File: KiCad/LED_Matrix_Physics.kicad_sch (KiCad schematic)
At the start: 3 parts

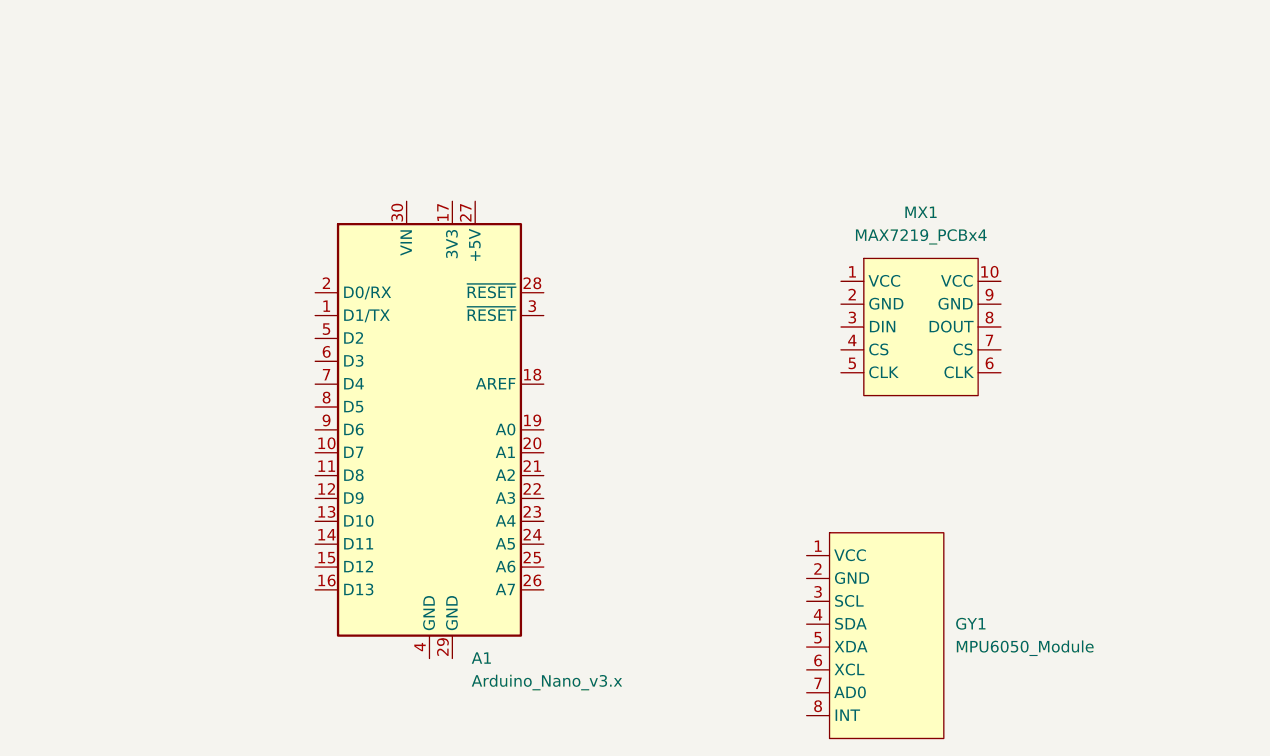
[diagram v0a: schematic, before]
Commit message: Created KiCad schematic
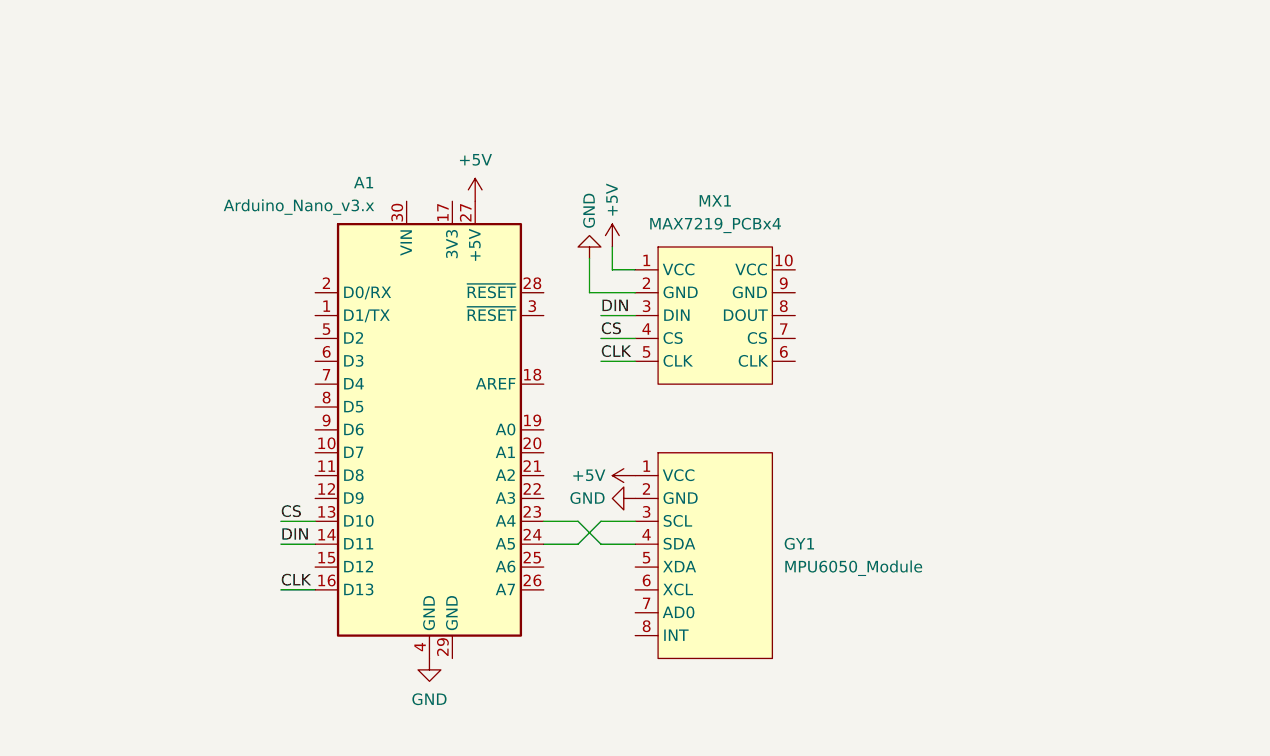
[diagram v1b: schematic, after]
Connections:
- net CS: now reaches A1.13 (D10)
- net CS: now also MX1.4 (CS)
- net DIN: now reaches A1.14 (D11)
- net DIN: now also MX1.3 (DIN)
- net CLK: now reaches A1.16 (D13)
- net CLK: now also MX1.5 (CLK)
- net at A1.23 (A4): now also GY1.4 (SDA)
- net at A1.24 (A5): now also GY1.3 (SCL)
- net +5V: now reaches A1.27 (+5V)
- net +5V: now also GY1.1 (VCC), MX1.1 (VCC)
- net GND: now reaches A1.4 (GND)
- net GND: now also GY1.2 (GND), MX1.2 (GND)
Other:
- moved on the sheet: GY1, MX1

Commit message: Added battery to schematic
Added a battery, diode for inverse polarity protection, and a switch for the battery to the schematic.
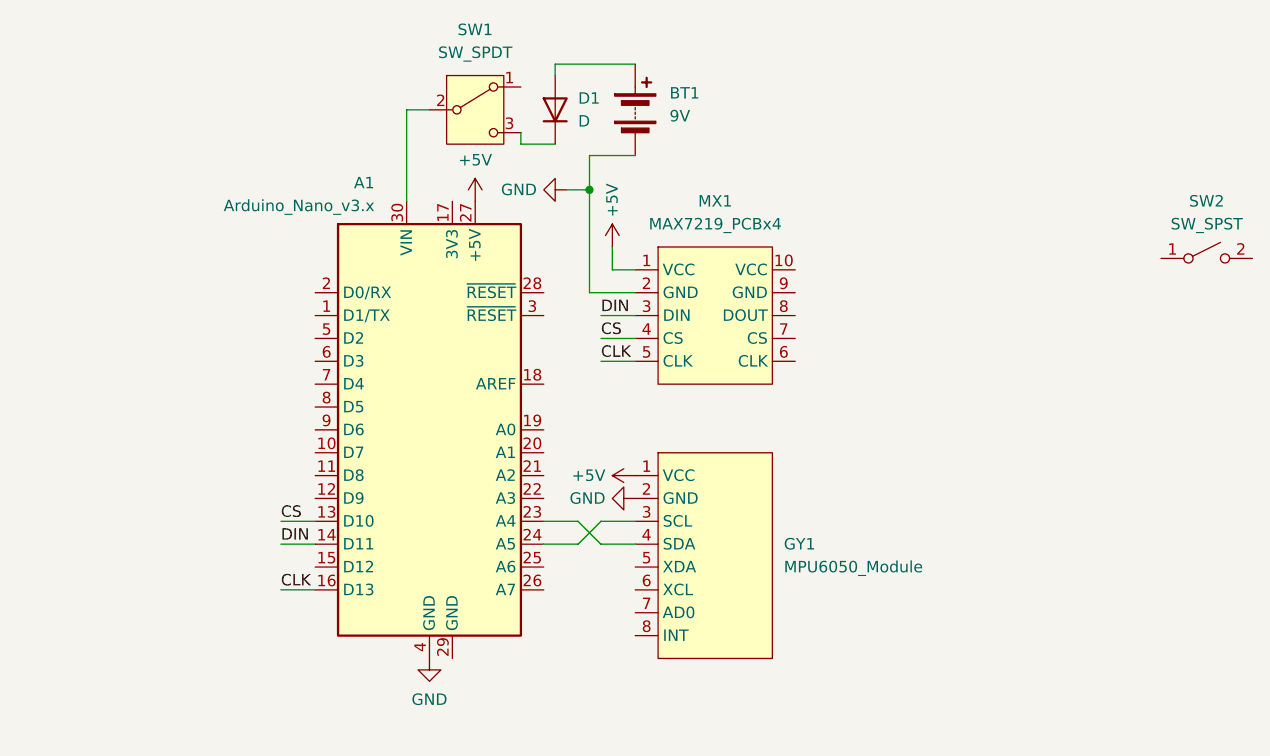
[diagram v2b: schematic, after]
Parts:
- added BT1: 9V, symbol Device:Battery
- added D1: D, symbol Device:D
- added SW1: SW_SPDT, symbol Switch:SW_SPDT
- added SW2: SW_SPST, symbol Switch:SW_SPST
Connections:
- net GND: now also BT1.2 (-)
- net at A1.30 (VIN): now also SW1.2 (B)
- new net: D1.1 (K), SW1.3 (C)
- new net: BT1.1 (+), D1.2 (A)

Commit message: Moved battery diode in schematic
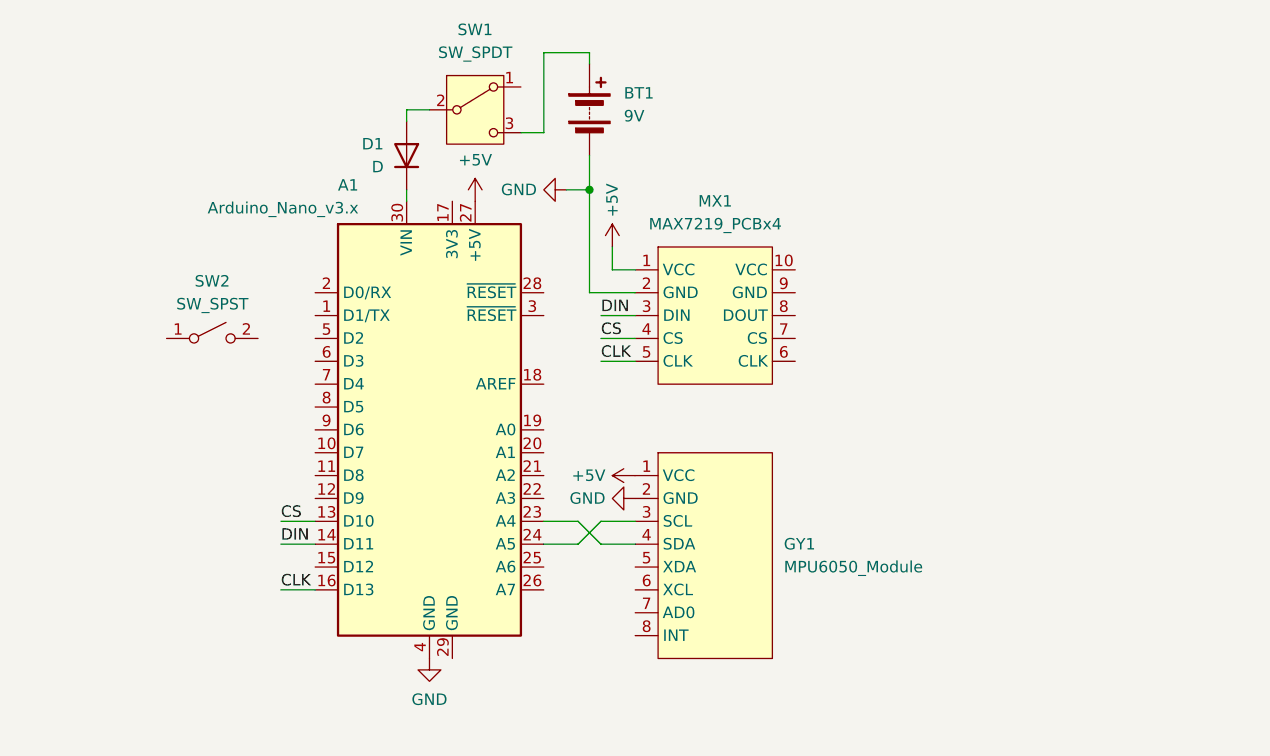
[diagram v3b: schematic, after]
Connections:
- net at A1.30 (VIN): now also D1.1 (K); no longer SW1.2 (B)
- net at SW1.3 (C): now also BT1.1 (+); no longer D1.1 (K)
- net at D1.2 (A): now also SW1.2 (B); no longer BT1.1 (+)
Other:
- moved on the sheet: BT1, D1, SW2
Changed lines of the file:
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@@
-	(wire
-		(pts
-			(xy 57.15 49.53) (xy 54.61 49.53)
-		)
-		(stroke
-			(width 0)
-			(type default)
-		)
-	)
 	(wire
 		(pts
@@
 	(wire
 		(pts
+			(xy 54.61 49.53) (xy 57.15 49.53)
+		)
+		(stroke
+			(width 0)
+			(type default)
+		)
+	)
+	(wire
+		(pts
 			(xy 76.2 72.39) (xy 80.01 72.39)
 		)
@@
 	(wire
 		(pts
-			(xy 80.01 44.45) (xy 71.12 44.45)
+			(xy 74.93 43.18) (xy 69.85 43.18)
 		)
 		(stroke
@@
 	(wire
 		(pts
-			(xy 67.31 53.34) (xy 67.31 52.07)
+			(xy 54.61 58.42) (xy 54.61 59.69)
+		)
+		(stroke
+			(width 0)
+			(type default)
+		)
+	)
+	(wire
+		(pts
+			(xy 74.93 43.18) (xy 74.93 44.45)
 		)
 		(stroke
@@
 	(wire
 		(pts
-			(xy 71.12 44.45) (xy 71.12 45.72)
+			(xy 69.85 43.18) (xy 69.85 52.07)
+		)
+		(stroke
+			(width 0)
+			(type default)
+		)
+	)
+	(wire
+		(pts
+			(xy 54.61 50.8) (xy 54.61 49.53)
 		)
 		(stroke
@@
 	(wire
 		(pts
-			(xy 54.61 49.53) (xy 54.61 59.69)
-		)
-		(stroke
-			(width 0)
-			(type default)
-		)
-	)
-	(wire
-		(pts
-			(xy 80.01 54.61) (xy 74.93 54.61)
-		)
-		(stroke
-			(width 0)
-			(type default)
-		)
-	)
-	(wire
-		(pts
-			(xy 71.12 53.34) (xy 67.31 53.34)
+			(xy 69.85 52.07) (xy 67.31 52.07)
 		)
 		(stroke
@@
 		(dnp no)
 		(property "Reference" "A1"
-			(at 51.054 57.658 0)
+			(at 49.276 57.912 0)
 			(show_name no)
 			(do_not_autoplace no)
@@
 		)
 		(property "Value" "Arduino_Nano_v3.x"
-			(at 51.054 60.198 0)
+			(at 49.276 60.452 0)
 			(show_name no)
 			(do_not_autoplace no)
@@
 	(symbol
 		(lib_id "Device:D")
-		(at 71.12 49.53 90)
+		(at 54.61 54.61 270)
+		(mirror x)
 		(unit 1)
 		(body_style 1)
@@
 		(in_pos_files yes)
 		(dnp no)
-		(fields_autoplaced yes)
 		(property "Reference" "D1"
-			(at 73.66 48.2599 90)
+			(at 52.07 53.3399 90)
 			(show_name no)
 			(do_not_autoplace no)
@@
 		)
 		(property "Value" "D"
-			(at 73.66 50.7999 90)
+			(at 52.07 55.8799 90)
 			(show_name no)
 			(do_not_autoplace no)
@@
 		)
 		(property "Footprint" ""
-			(at 71.12 49.53 0)
+			(at 54.61 54.61 0)
 			(hide yes)
 			(show_name no)
@@
 		)
 		(property "Datasheet" ""
-			(at 71.12 49.53 0)
+			(at 54.61 54.61 0)
 			(hide yes)
 			(show_name no)
@@
 		)
 		(property "Description" "Diode"
-			(at 71.12 49.53 0)
+			(at 54.61 54.61 0)
 			(hide yes)
 			(show_name no)
@@
 		)
 		(property "Sim.Device" "D"
-			(at 71.12 49.53 0)
+			(at 54.61 54.61 0)
 			(hide yes)
 			(show_name no)
@@
 		)
 		(property "Sim.Pins" "1=K 2=A"
-			(at 71.12 49.53 0)
+			(at 54.61 54.61 0)
 			(hide yes)
 			(show_name no)
@@
 	(symbol
 		(lib_id "Device:Battery")
-		(at 80.01 49.53 0)
+		(at 74.93 49.53 0)
 		(unit 1)
 		(body_style 1)
@@
 		(dnp no)
 		(property "Reference" "BT1"
-			(at 83.82 47.6884 0)
+			(at 78.74 47.6884 0)
 			(show_name no)
 			(do_not_autoplace no)
@@
 		)
 		(property "Value" "9V"
-			(at 83.82 50.2284 0)
+			(at 78.74 50.2284 0)
 			(show_name no)
 			(do_not_autoplace no)
@@
 		)
 		(property "Footprint" ""
-			(at 80.01 48.006 90)
+			(at 74.93 48.006 90)
 			(hide yes)
 			(show_name no)
@@
 		)
 		(property "Datasheet" ""
-			(at 80.01 48.006 90)
+			(at 74.93 48.006 90)
 			(hide yes)
 			(show_name no)
@@
 		)
 		(property "Description" "Multiple-cell battery"
-			(at 80.01 49.53 0)
+			(at 74.93 49.53 0)
 			(hide yes)
 			(show_name no)
@@
 		)
 		(property "Sim.Device" "V"
-			(at 80.01 49.53 0)
+			(at 74.93 49.53 0)
 			(hide yes)
 			(show_name no)
@@
 		)
 		(property "Sim.Type" "DC"
-			(at 80.01 49.53 0)
+			(at 74.93 49.53 0)
 			(hide yes)
 			(show_name no)
@@
 		)
 		(property "Sim.Pins" "1=+ 2=-"
-			(at 80.01 49.53 0)
+			(at 74.93 49.53 0)
 			(hide yes)
 			(show_name no)
@@
 	(symbol
 		(lib_id "Switch:SW_SPST")
-		(at 143.51 66.04 0)
+		(at 33.02 74.93 0)
 		(unit 1)
 		(body_style 1)
@@
 		(fields_autoplaced yes)
 		(property "Reference" "SW2"
-			(at 143.51 59.69 0)
+			(at 33.02 68.58 0)
 			(show_name no)
 			(do_not_autoplace no)
@@
 		)
 		(property "Value" "SW_SPST"
-			(at 143.51 62.23 0)
+			(at 33.02 71.12 0)
 			(show_name no)
 			(do_not_autoplace no)
@@
 		)
 		(property "Footprint" ""
-			(at 143.51 66.04 0)
+			(at 33.02 74.93 0)
 			(hide yes)
 			(show_name no)
@@
 		)
 		(property "Datasheet" ""
-			(at 143.51 66.04 0)
+			(at 33.02 74.93 0)
 			(hide yes)
 			(show_name no)
@@
 		)
 		(property "Description" "Single Pole Single Throw (SPST) switch"
-			(at 143.51 66.04 0)
-			(hide yes)
-			(show_name no)
+			(at 33.02 74.93 0)
+			(hide yes)
+			(show_name no)

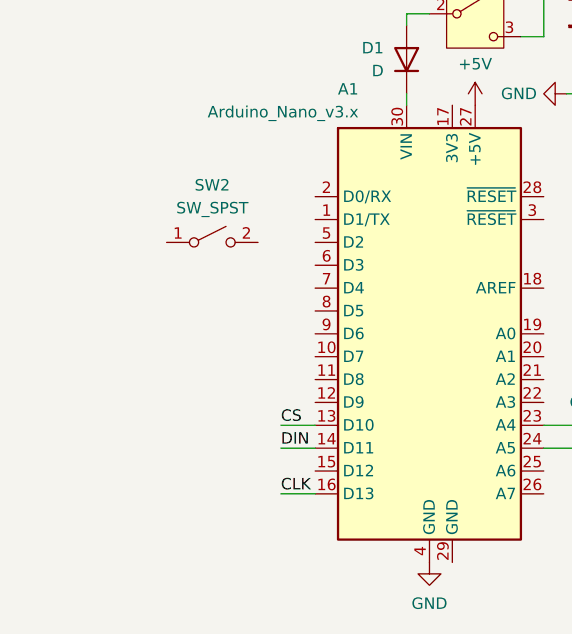
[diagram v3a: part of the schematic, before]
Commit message: Added push buttons to schematic
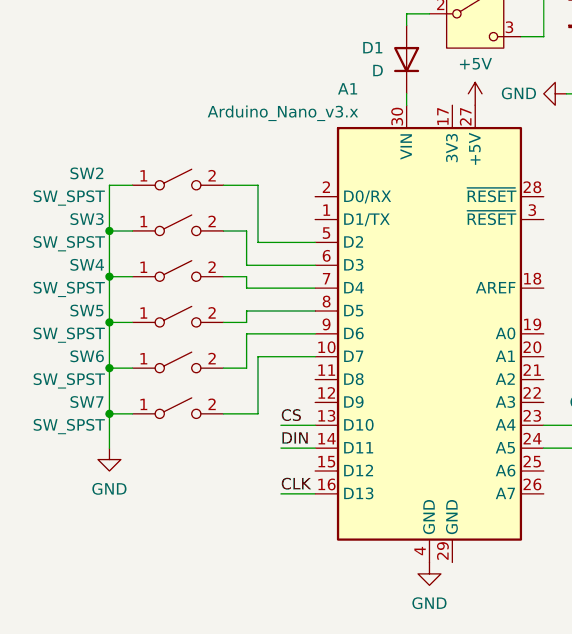
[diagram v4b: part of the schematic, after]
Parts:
- added SW3, SW4, SW5, SW6, SW7: SW_SPST, symbol Switch:SW_SPST
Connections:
- net GND: now also SW2.1 (A), SW3.1 (A), SW4.1 (A), SW5.1 (A), SW6.1 (A), SW7.1 (A)
- net at A1.10 (D7): now also SW7.2 (B)
- net at A1.5 (D2): now also SW2.2 (B)
- net at A1.6 (D3): now also SW3.2 (B)
- net at A1.7 (D4): now also SW4.2 (B)
- net at A1.8 (D5): now also SW5.2 (B)
- net at A1.9 (D6): now also SW6.2 (B)
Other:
- moved on the sheet: SW2
